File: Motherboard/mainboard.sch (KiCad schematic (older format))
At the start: 55 parts, among them IC1 BMX160, J1 Conn_01x01, J2 10118194-0001LF, J28 Conn_01x01, J29 Conn_01x01, J3 Micro_SD_Card, J30 Conn_01x01, J5 XF2M-1015-1A, J6 U.FL-R-SMT-1, J7 U.FL-R-SMT-1, J8 Conn_01x01, J9 XF2M36151A, SW1 KMR231NG LFS, U1 RFM95W-915S2, U2 ATSAMD51G_TQFN48, U3 DRV8848, U4 TPS82740BSIPR, U5 DRV8848, U6 MAX708RESA-T, U8 RFM95W-915S2

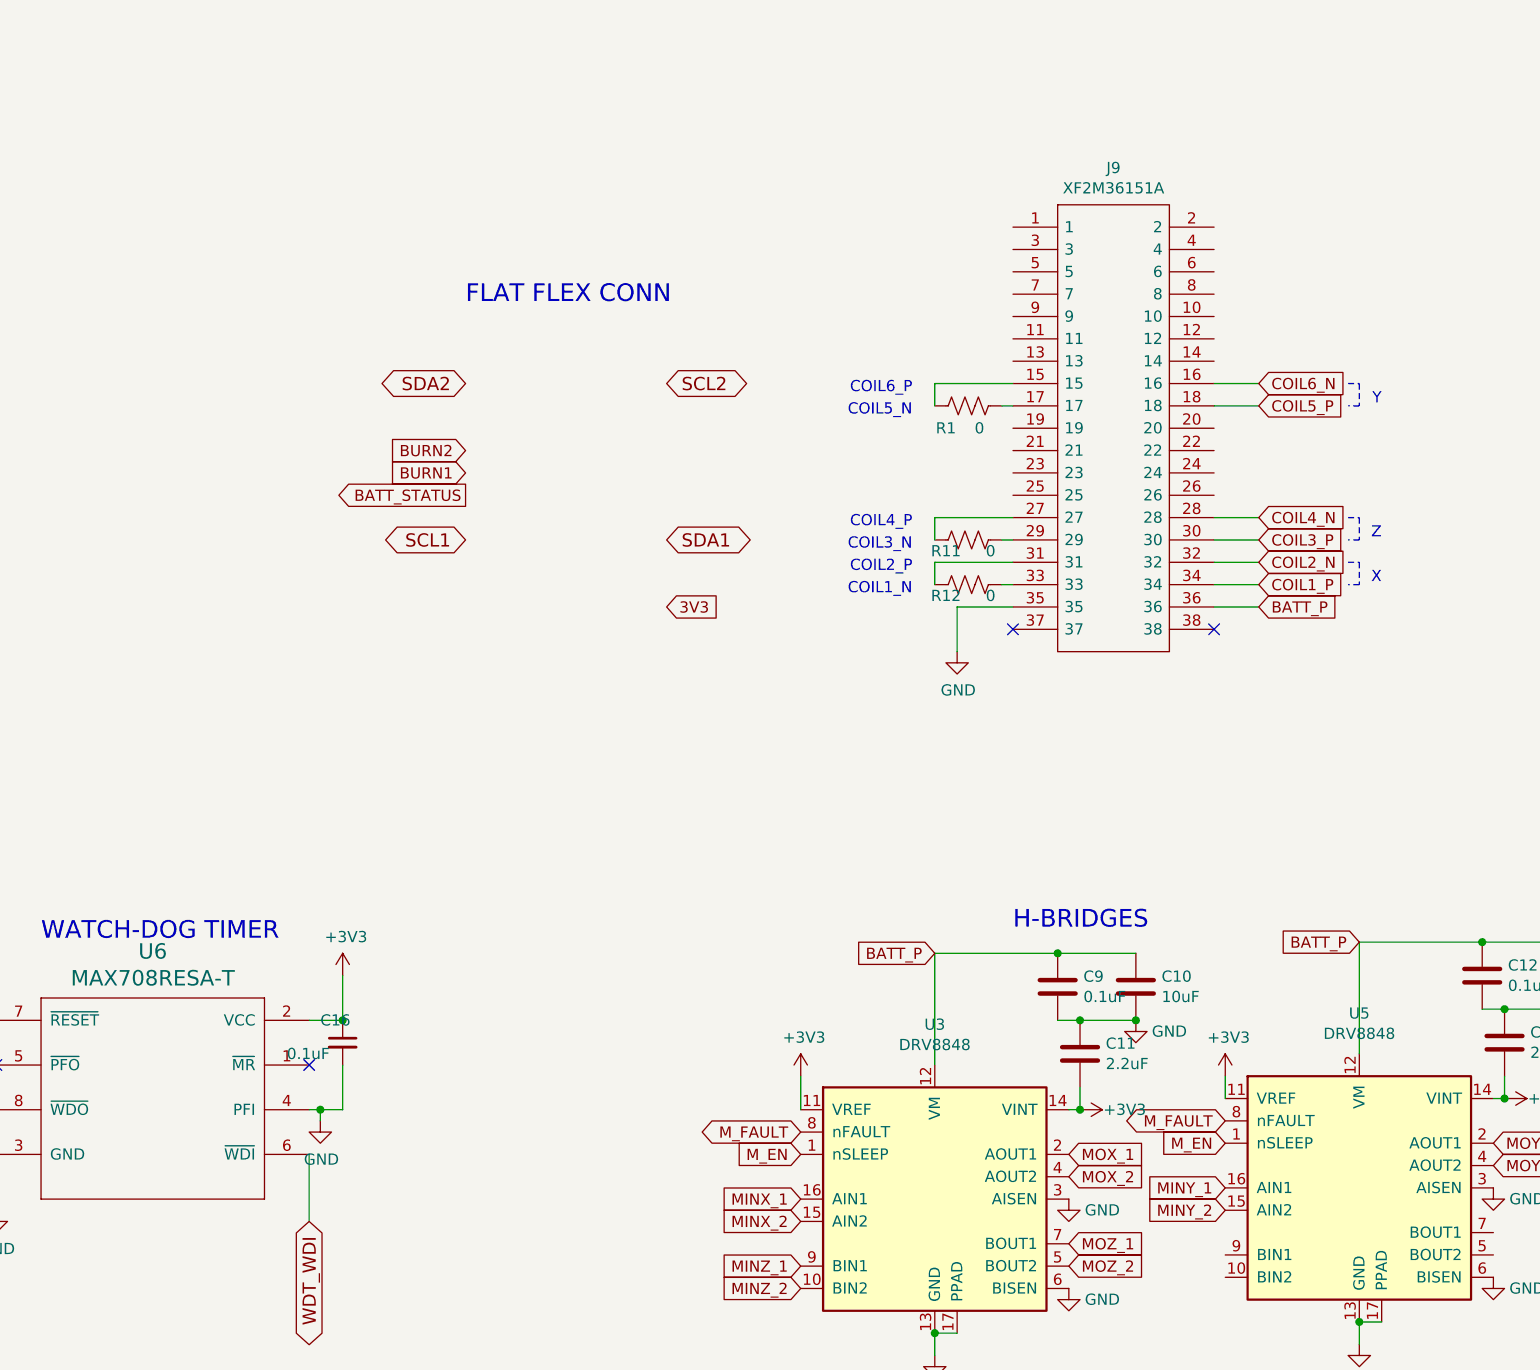
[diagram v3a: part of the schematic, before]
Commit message: big FPC routed
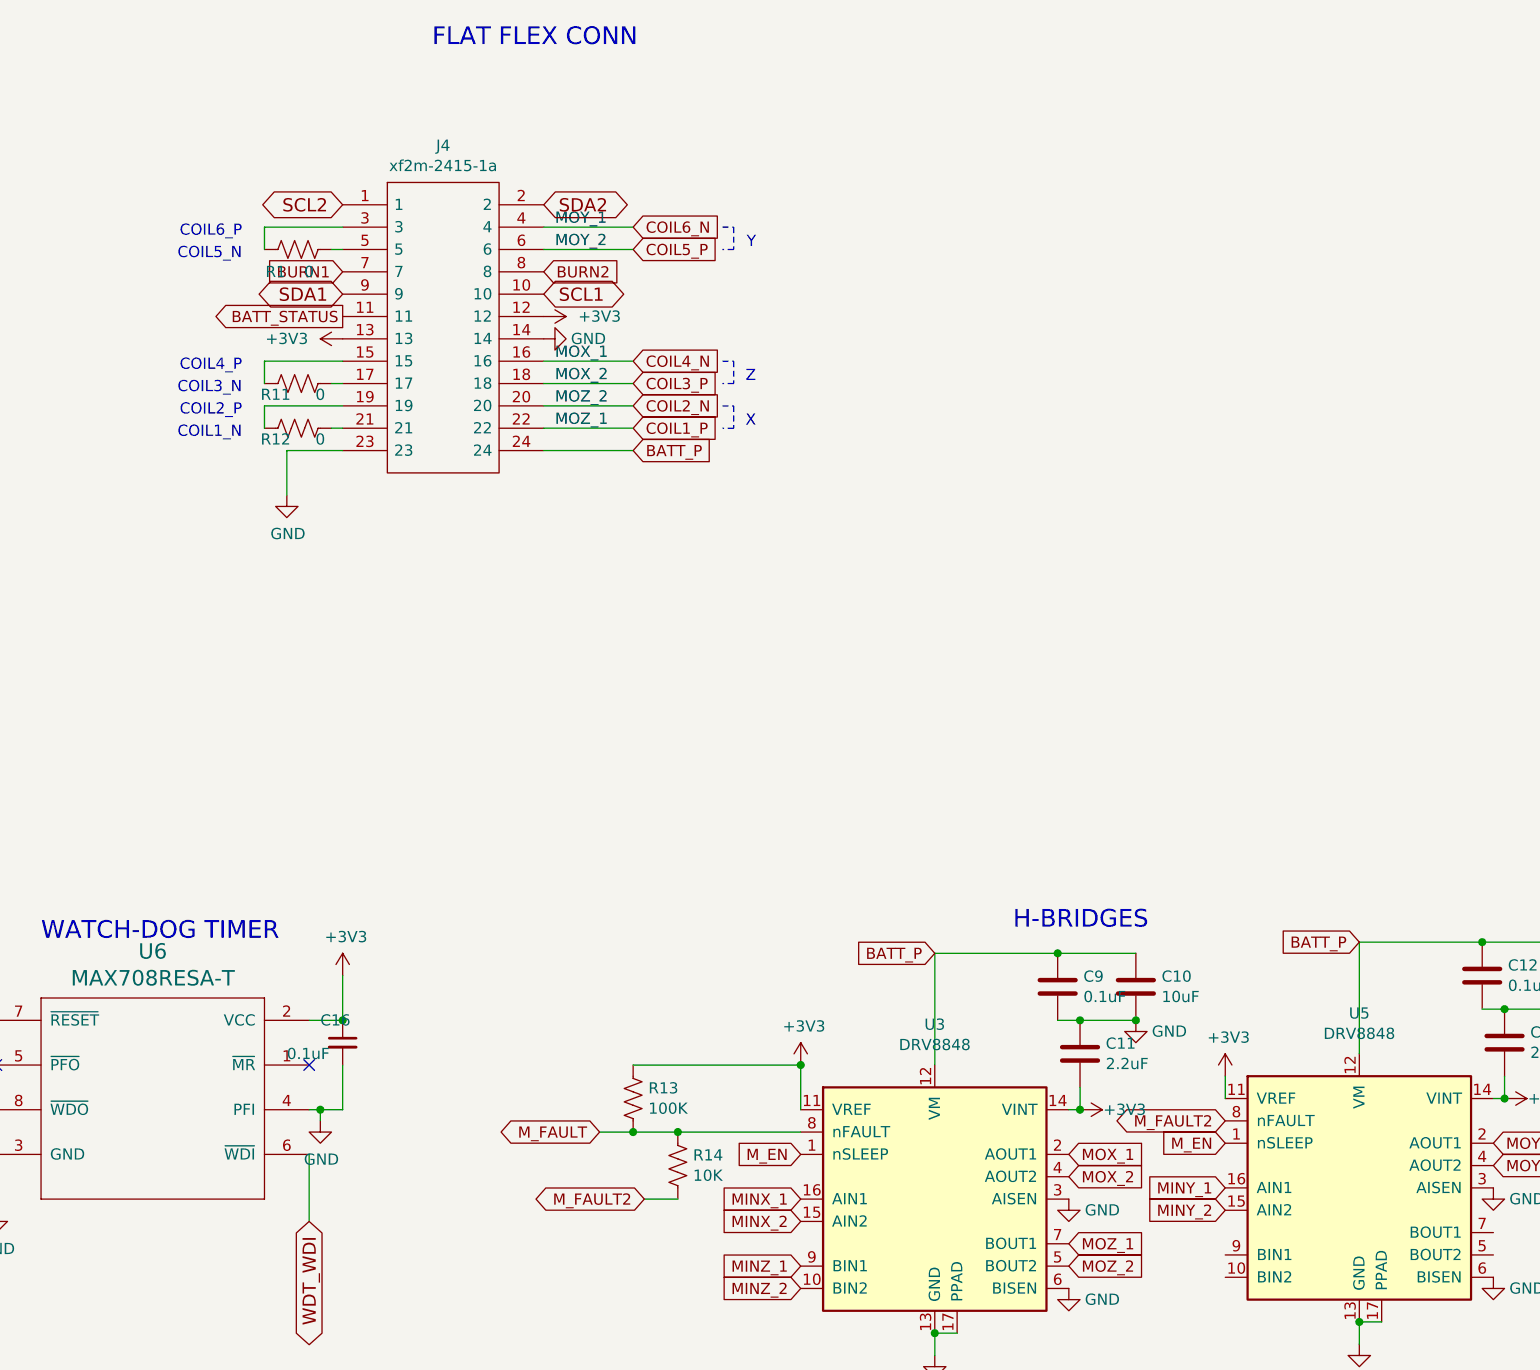
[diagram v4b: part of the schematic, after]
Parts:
- removed J9: XF2M36151A, custom-footprints:XF2M36151A, symbol symbols:XF2M36151A
- added J4: xf2m-2415-1a, custom-footprints:XF2M-2415-1A, symbol symbols:xf2m-2415-1a
- added R13: 100K, Resistor_SMD:R_0402_1005Metric, symbol mainboard-rescue:R_US-Device
- added R14: 10K, Resistor_SMD:R_0402_1005Metric, symbol mainboard-rescue:R_US-Device
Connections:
- net MOX_1 is gone; now on net COIL4_N: U3.2 (AOUT1)
- net MOX_2 is gone; now on net COIL3_P: U3.4 (AOUT2)
- net MOY_1 is gone; now on net COIL6_N: U5.2 (AOUT1)
- net MOY_2 is gone; now on net COIL5_P: U5.4 (AOUT2)
- net MOZ_1 is gone; now on net COIL1_P: U3.7 (BOUT1)
- net MOZ_2 is gone; now on net COIL2_N: U3.5 (BOUT2)
- net +3V3: now also J4.12, J4.13, R13.2
- net BATT_P: now also J4.24
- net BATT_STATUS: now also J4.11
- net BURN1: now also J4.7
- net BURN2: now also J4.8
- net COIL1_P: now also J4.22
- net COIL2_N: now also J4.20
- net COIL3_P: now also J4.18
- net COIL4_N: now also J4.16
- net COIL5_P: now also J4.6
- net COIL6_N: now also J4.4
- net GND: now also J4.14, J4.23
- net M_FAULT: now also R13.1, R14.1; no longer U5.8 (nFAULT)
- net SCL1: now also J4.10
- net SCL2: now also J4.1
- net SDA1: now also J4.9
- net SDA2: now also J4.2
- net at R1.1: now also J4.3
- net at R1.2: now also J4.5
- net at R11.1: now also J4.15
- net at R11.2: now also J4.17
- net at R12.1: now also J4.19
- net at R12.2: now also J4.21
- new net M_FAULT2: R14.2, U5.8 (nFAULT)
- no-connect marks 13 -> 11
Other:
- moved on the sheet: R1, R11, R12
